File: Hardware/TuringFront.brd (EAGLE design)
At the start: 107 x 49.5 mm, 66 parts, among them T1 2N3904, U1 TL074_

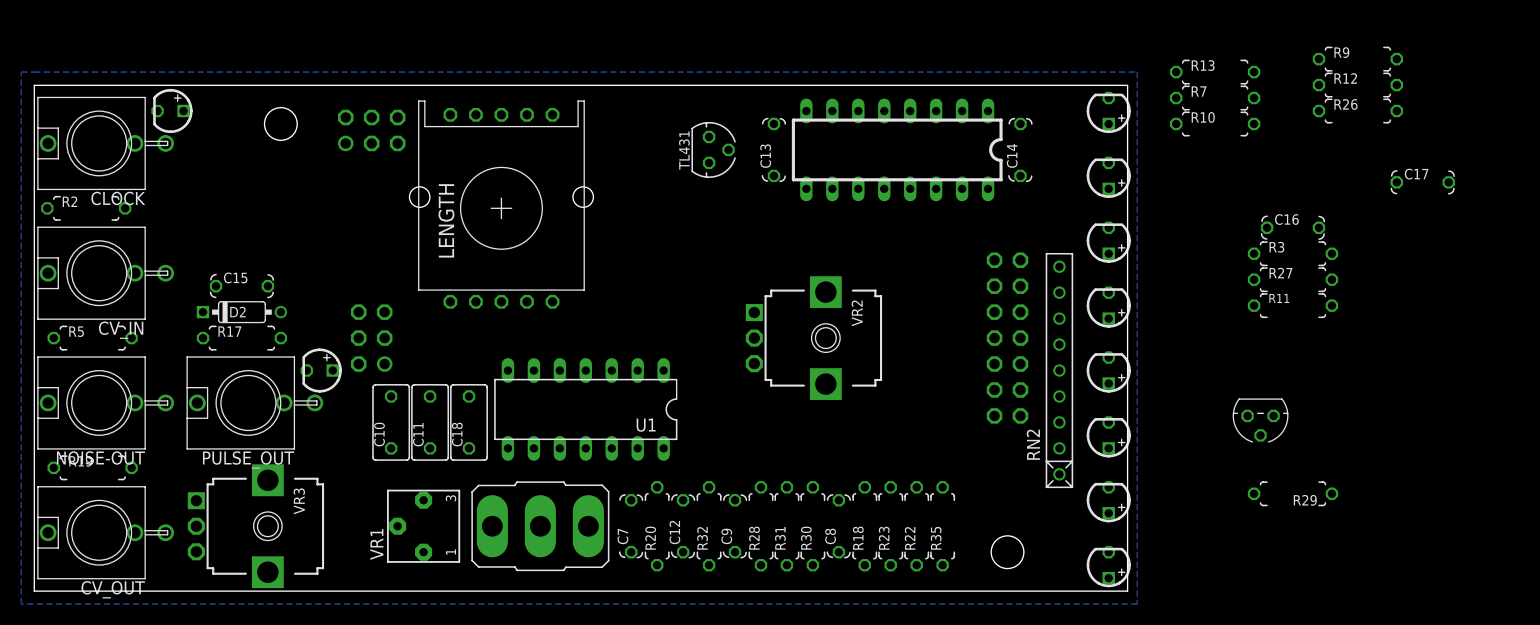
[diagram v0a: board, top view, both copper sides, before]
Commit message: Starting to route front board
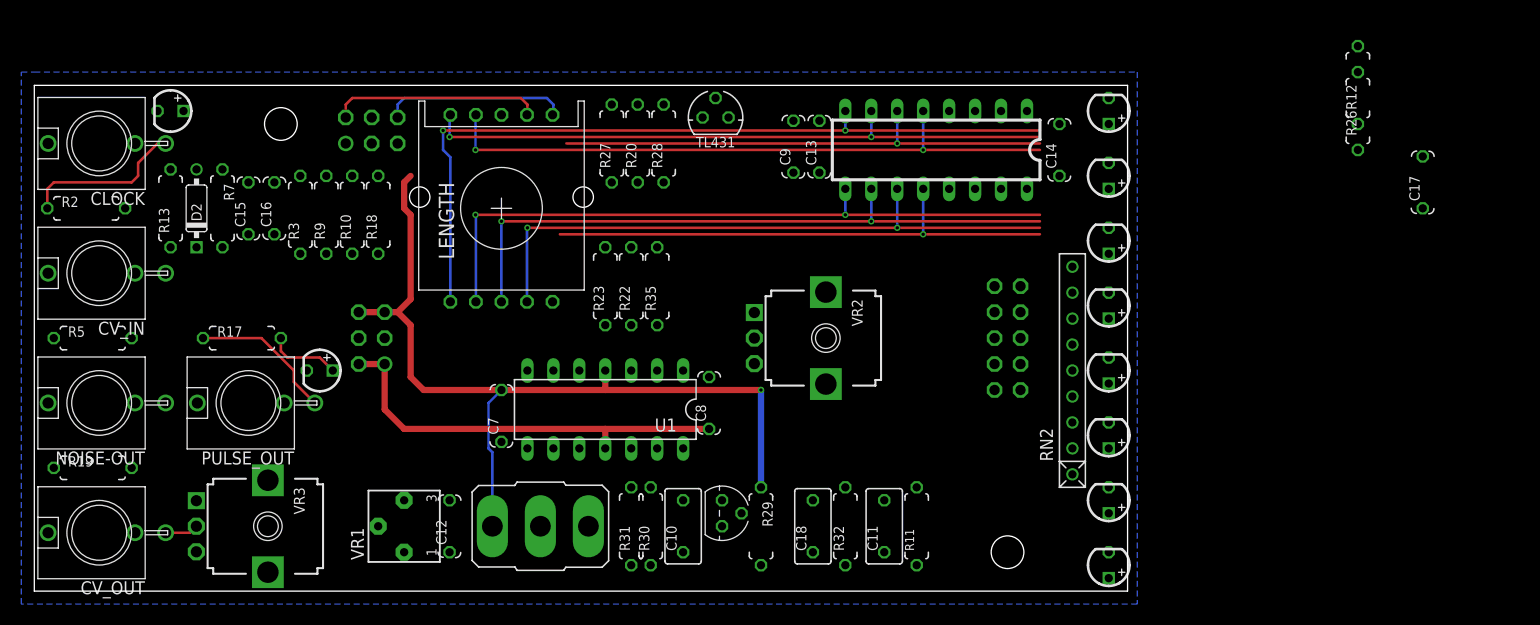
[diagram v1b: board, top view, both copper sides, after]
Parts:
- removed FRONT_BUS: (no value), MusicThingModular:MA07-2_BACKSIDE
- added SV1: (no value), MusicThingModular:10PIN_BACKSIDE
- moved R13 103.1 mm to (13.3, 37.5), turned to 90 degrees
- moved R9 102.1 mm to (28.6, 36.8), turned to 90 degrees
- moved C16 99.7 mm to (23.5, 37.5), turned to 90 degrees
- moved R7 97.8 mm to (18.4, 37.5), turned to 270 degrees
- moved R3 97.2 mm to (26.0, 36.8), turned to 90 degrees
- moved R10 84.9 mm to (31.1, 36.8), turned to 90 degrees
- moved R27 68.0 mm to (56.5, 43.8), turned to 90 degrees
- moved R18 56.5 mm to (33.7, 36.8)
- moved T1 53.6 mm to (67.3, 7.62), turned to 270 degrees
- moved R29 52.2 mm to (71.1, 6.35), turned to 270 degrees
- moved C11 45.6 mm to (83.2, 6.35)
- moved R11 42.7 mm to (86.4, 6.35), turned to 90 degrees
- moved R28 38.7 mm to (61.6, 43.8)
- moved C9 37.6 mm to (74.3, 43.5)
- moved R20 37.5 mm to (59.1, 43.8)
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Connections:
- net +12V_FRONT: now also C7.2, R20.1, R23.2, R29.1, R3.1; no longer C7.1, R20.2, R23.1, R29.2, R3.2
- net -12V_FRONT: now also C14.2, C8.1, C9.2, R35.2; no longer C14.1, C8.2, C9.1, R35.1
- net B1_FRONT: now also SV1.1; no longer FRONT_BUS.1
- net B2_FRONT: now also SV1.2; no longer FRONT_BUS.2
- net B3_FRONT: now also SV1.3; no longer FRONT_BUS.3
- net B4_FRONT: now also SV1.4; no longer FRONT_BUS.4
- net B5_FRONT: now also SV1.5; no longer FRONT_BUS.5
- net B6_FRONT: now also SV1.6; no longer FRONT_BUS.6
- net B7_FRONT: now also SV1.7; no longer FRONT_BUS.7
- net B8_FRONT: now also SV1.8; no longer FRONT_BUS.8
- net CLOCK_FRONT: now also R13.1, SV1.9; no longer FRONT_BUS.9, R13.2
- net GND_FRONT: now also C14.1, C16.1, C7.1, C8.2, R11.1, R9.1, U1.12; no longer C14.2, C16.2, C7.2, C8.1, R11.2, R9.2, U1.5
- net LOOP_CTRL_FRONT: now also R22.2; no longer R22.1
- net MAIN_OUT: now also U1.1; no longer U1.8
- net N$12: now also C16.2, R3.2, R9.2, U1.6; no longer C16.1, R3.1, R9.1, U1.13
- net N$13: now also U1.2; no longer U1.9
- net N$15: now also R13.2; no longer R13.1
- net N$16: now also C10.2, R29.2; no longer C10.1, R29.1
- net N$18: now also R20.2, R28.2; no longer R20.1, R28.1
- net N$20: now also C10.1; no longer C10.2
- net N$21: now also U1.9; no longer U1.2
- net N$22: now also U1.8; no longer U1.1
- net N$25: now also C9.1; no longer C9.2
- net N$26: now also R28.1; no longer R28.2
- net N$27: now also R32.1, U1.13; no longer R32.2, U1.6
- net N$41: now also U1.14; no longer U1.7
- net N$43: now also R22.1; no longer R22.2
- net N$47: now also R23.1; no longer R23.2
- net N$48: now also R35.1; no longer R35.2
- net N$5: now also U1.5; no longer U1.12
- net N$6: now also R17.2; no longer R17.1
- net N$8: now also U1.7; no longer U1.14
- net N$9: now also R32.2; no longer R32.1
- net NOISE_FRONT: now also R11.2; no longer R11.1
- net PULSE_OUT_FRONT: now also R17.1, SV1.10; no longer FRONT_BUS.10, R17.2
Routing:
- net +12V_FRONT: track 0.00 -> 85.3 mm, vias 0 -> 1
- net B4_FRONT: track 0.00 -> 77.4 mm, vias 0 -> 2
- net B5_FRONT: track 0.00 -> 66.3 mm, vias 0 -> 2
- net B6_FRONT: track 0.00 -> 63.8 mm, vias 0 -> 2
- net B3_FRONT: track 0.00 -> 62.5 mm, vias 0 -> 2
- net B1_FRONT: track 0.00 -> 62.5 mm, vias 0 -> 2
- net B7_FRONT: track 0.00 -> 61.2 mm, vias 0 -> 2
- net B8_FRONT: track 0.00 -> 51.4 mm, vias 0 -> 1
- net B2_FRONT: track 0.00 -> 49.5 mm, vias 0 -> 1
- net -12V_FRONT: track 0.00 -> 41.4 mm
- net STEP_16_FRONT: track 0.00 -> 20.6 mm
- net END_OF_LOOP_FRONT: track 0.00 -> 18.1 mm
- net N$2: track 0.00 -> 16.1 mm
- net PULSE_OUT_FRONT: track 0.00 -> 14.2 mm
- net N$6: track 0.00 -> 7.14 mm
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
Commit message: Layouts
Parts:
- removed RN2: 2.2k, resistor-net:RN-9
- added R1, R14, R15, R16, R21, R4, R6, R8: 2.2k, TomW:0207/7
- moved R12 111.8 mm to (18.4, 37.5)
- moved C7 73.4 mm to (116.2, 37.5)
- moved C13 70.5 mm to (144.1, 22.5)
- moved TL431 70.5 mm to (134.0, 25.4)
- moved R20 70.5 mm to (126.4, 22.9)
- moved R27 70.5 mm to (123.8, 22.9)
- moved R28 70.5 mm to (128.9, 22.9)
- moved C9 70.5 mm to (141.6, 22.5)
- moved R29 59.7 mm to (130.8, 7.62)
- moved C10 59.1 mm to (122.6, 7.62)
- moved T1 59.1 mm to (126.4, 8.89)
- moved R30 58.4 mm to (118.7, 7.62)
- moved C8 58.0 mm to (120.7, 38.1)
- moved C18 57.8 mm to (134.0, 7.62)
- moved R11 57.8 mm to (144.1, 7.62)
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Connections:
- net CLOCK_FRONT: now also R12.1, R7.1; no longer R12.2, R7.2
- net GND_FRONT: now also R1.2, R12.2, R14.1, R15.1, R16.1, R21.1, R4.2, R6.2, R8.2; no longer R12.1, RN2.1
- net N$30: now also R1.1; no longer RN2.9
- net N$31: now also R4.1; no longer RN2.8
- net N$32: now also R6.1; no longer RN2.7
- net N$33: now also R8.1; no longer RN2.6
- net N$34: now also R14.2; no longer RN2.5
- net N$35: now also R15.2; no longer RN2.4
- net N$36: now also R16.2; no longer RN2.3
- net N$37: now also R21.2; no longer RN2.2
- net N$5: now also R7.2; no longer R7.1
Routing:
- net +12V_FRONT: track 85.3 -> 0.00 mm, vias 1 -> 0
- net B4_FRONT: track 77.4 -> 0.00 mm, vias 2 -> 0
- net B5_FRONT: track 66.3 -> 0.00 mm, vias 2 -> 0
- net B6_FRONT: track 63.8 -> 0.00 mm, vias 2 -> 0
- net B3_FRONT: track 62.5 -> 0.00 mm, vias 2 -> 0
- net B1_FRONT: track 62.5 -> 0.00 mm, vias 2 -> 0
- net B7_FRONT: track 61.2 -> 0.00 mm, vias 2 -> 0
- net MAIN_OUT: track 0.00 -> 60.0 mm
- net B8_FRONT: track 51.4 -> 0.00 mm, vias 1 -> 0
- net PULSE_OUT_FRONT: track 14.2 -> 65.5 mm
- net B2_FRONT: track 49.5 -> 0.00 mm, vias 1 -> 0
- net -12V_FRONT: track 41.4 -> 0.00 mm
- net LOOP_CTRL_FRONT: track 0.00 -> 30.5 mm
- net NOISE_FRONT: track 0.00 -> 23.8 mm
- net STEP_16_FRONT: track 20.6 -> 0.00 mm
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
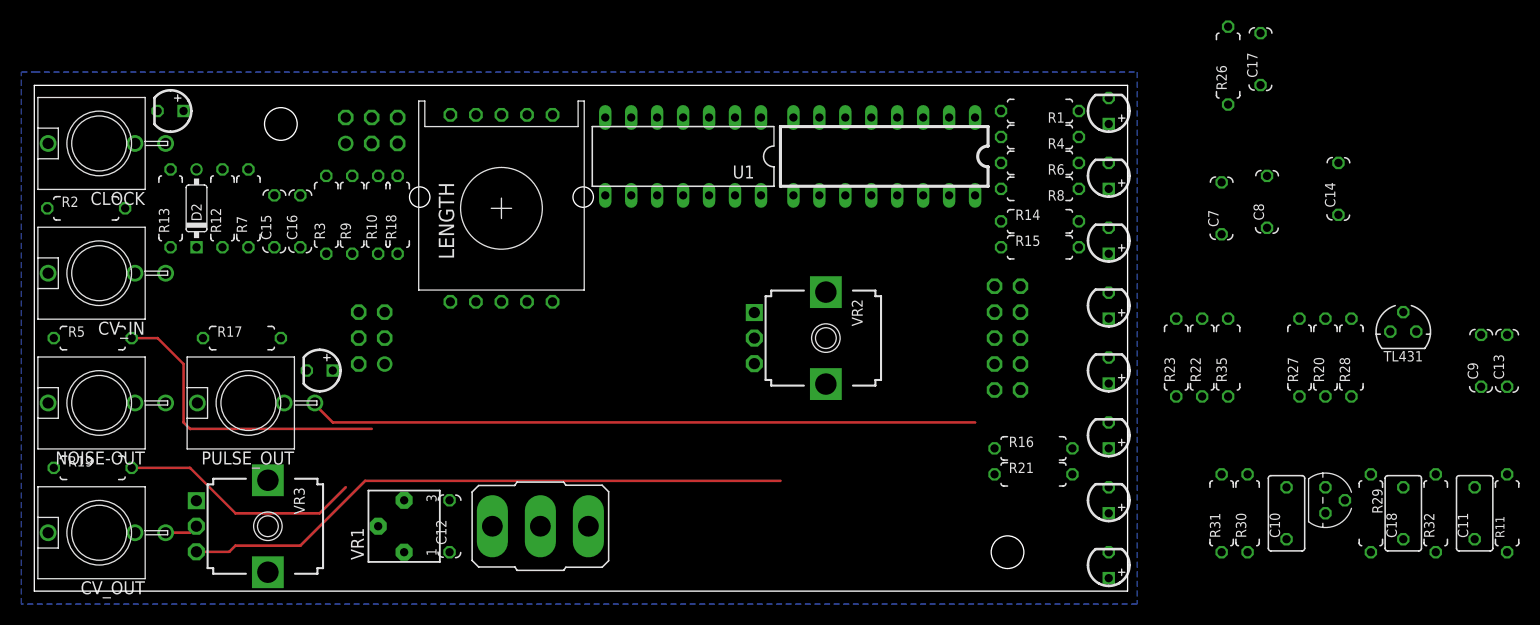
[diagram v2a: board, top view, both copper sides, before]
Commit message: routing tweaks on back panel
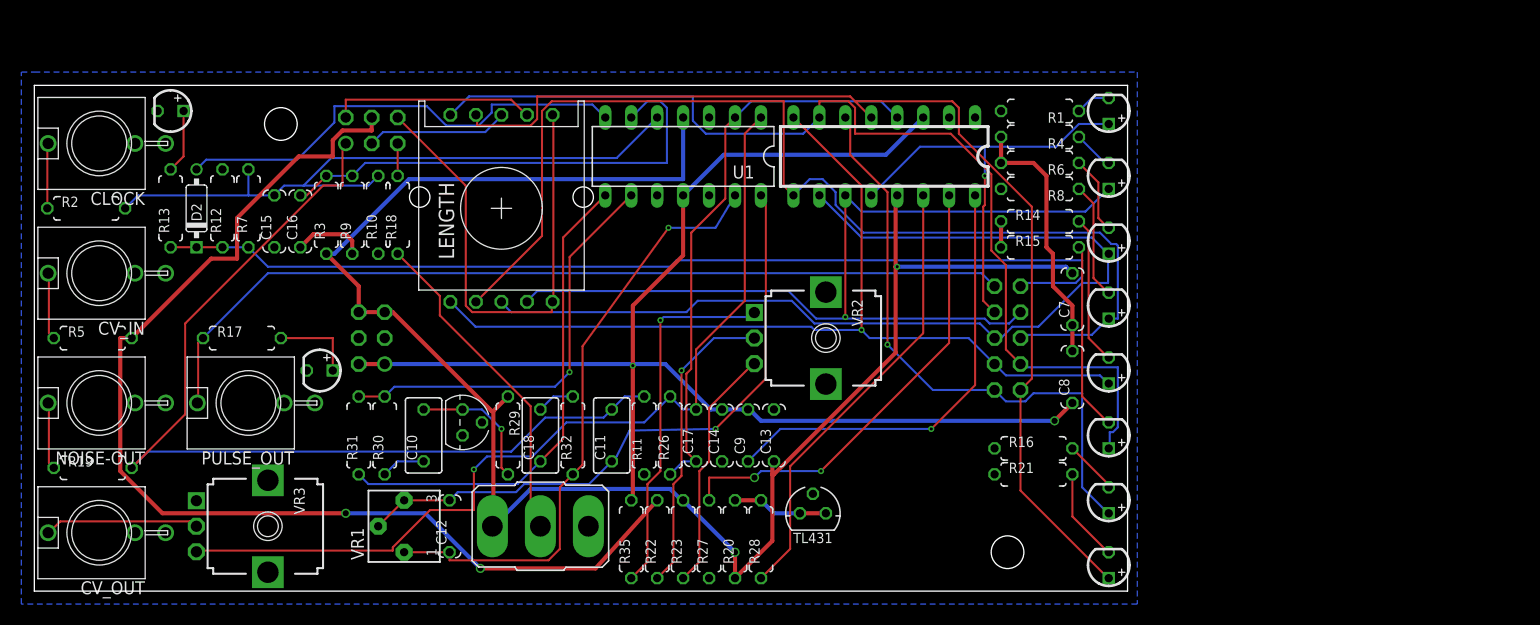
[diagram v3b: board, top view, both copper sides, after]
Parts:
- moved C10 84.8 mm to (38.1, 15.2)
- moved C18 84.8 mm to (49.5, 15.2)
- moved R11 84.8 mm to (59.7, 15.2)
- moved R29 84.8 mm to (46.4, 15.2)
- moved R30 84.8 mm to (34.3, 15.2)
- moved C11 84.8 mm to (56.5, 15.2)
- moved R31 84.8 mm to (31.8, 15.2)
- moved R32 84.8 mm to (52.7, 15.2)
- moved T1 84.8 mm to (41.9, 16.5)
- moved C13 72.1 mm to (72.4, 15.2)
- moved C9 72.1 mm to (69.8, 15.2)
- moved C17 66.4 mm to (64.8, 15.2)
- moved R26 65.5 mm to (62.2, 15.2)
- moved C14 65.0 mm to (67.3, 15.2)
- moved R35 61.1 mm to (58.4, 5.08)
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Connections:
- net GND_FRONT: now also CLOCK.P$3_SLEEVE, CV_IN.P$3_SLEEVE, CV_OUT.P$3_SLEEVE, NOISE-OUT.P$3_SLEEVE, PULSE_OUT.P$3_SLEEVE, VR2.CHASSIS2, VR3.CHASSIS2; no longer CLOCK.P$1, CV_IN.P$1, CV_OUT.P$1, NOISE-OUT.P$1, PULSE_OUT.P$1, VR2.M1, VR2.M2, VR3.M1, VR3.M2
- net N$2: now also CLOCK.P$1_TIP; no longer CLOCK.P$3
- net N$3: now also CV_IN.P$1_TIP; no longer CV_IN.P$3
- net N$39: now also CV_OUT.P$1_TIP; no longer CV_OUT.P$3
- net N$40: now also NOISE-OUT.P$1_TIP; no longer NOISE-OUT.P$3
- net PULSE_OUT_FRONT: now also PULSE_OUT.P$1_TIP; no longer PULSE_OUT.P$3
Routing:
- net +12V_FRONT: track 0.00 -> 175.0 mm, vias 0 -> 2
- net -12V_FRONT: track 0.00 -> 131.6 mm, vias 0 -> 2
- net B5_FRONT: track 0.00 -> 108.3 mm
- net B1_FRONT: track 0.00 -> 106.5 mm
- net B3_FRONT: track 0.00 -> 101.2 mm
- net CLOCK_FRONT: track 0.00 -> 98.3 mm
- net B6_FRONT: track 0.00 -> 97.6 mm
- net B4_FRONT: track 0.00 -> 91.3 mm, vias 0 -> 1
- net B7_FRONT: track 0.00 -> 90.0 mm, vias 0 -> 1
- net LOOP_CTRL_FRONT: track 30.5 -> 110.0 mm, vias 0 -> 2
- net NOISE_FRONT: track 23.8 -> 94.6 mm
- net N$5: track 0.00 -> 66.0 mm
- net N$41: track 0.00 -> 62.5 mm, vias 0 -> 1
- net N$27: track 0.00 -> 59.9 mm, vias 0 -> 1
- net B2_FRONT: track 0.00 -> 58.5 mm, vias 0 -> 1
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
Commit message: Front board routed awaiting checking and optimisation
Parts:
- moved C8 26.2 mm to (98.4, 47.0), turned to 0 degrees
- moved R15 19.7 mm to (97.8, 14.0)
- moved R14 19.7 mm to (97.8, 16.5)
- moved C7 16.2 mm to (98.4, 44.5), turned to 180 degrees
- moved R1 5.08 mm to (98.4, 41.9)
- moved R4 5.08 mm to (98.4, 39.4)
- moved R6 5.08 mm to (98.4, 36.8)
- moved R8 5.08 mm to (98.4, 34.3)
- moved R16 2.54 mm to (97.8, 11.4)
- moved R21 2.54 mm to (97.8, 8.89)
- moved T1 1.90 mm to (41.9, 18.4), turned to 0 degrees
- moved C10 1.27 mm to (36.8, 15.2)
- moved R20 1.27 mm to (69.8, 5.08)
- moved R22 1.27 mm to (62.2, 5.08)
- moved R23 1.27 mm to (64.8, 5.08)
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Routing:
- net B5_FRONT: track 108.3 -> 81.2 mm, vias 0 -> 3
- net GND_FRONT: track 35.4 -> 9.72 mm
- net N$11: track 32.5 -> 48.0 mm
- net N$35: track 18.4 -> 4.61 mm
- net MAIN_OUT: track 89.5 -> 101.5 mm, vias 1 -> 3
- net END_OF_LOOP_FRONT: track 49.3 -> 37.4 mm
- net N$21: track 41.4 -> 53.0 mm
- net B7_FRONT: track 90.0 -> 78.7 mm, vias 1 -> 3
- net CLOCK_FRONT: track 98.3 -> 87.2 mm
- net B6_FRONT: track 97.6 -> 87.8 mm, vias 0 -> 3
- net LOOP_CTRL_FRONT: track 110.0 -> 100.3 mm
- net N$12: track 47.0 -> 38.0 mm
- net N$26: track 44.0 -> 51.0 mm, vias 0 -> 1
- net N$25: track 43.9 -> 50.7 mm
- net B8_FRONT: track 42.9 -> 49.3 mm, vias 1 -> 2
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
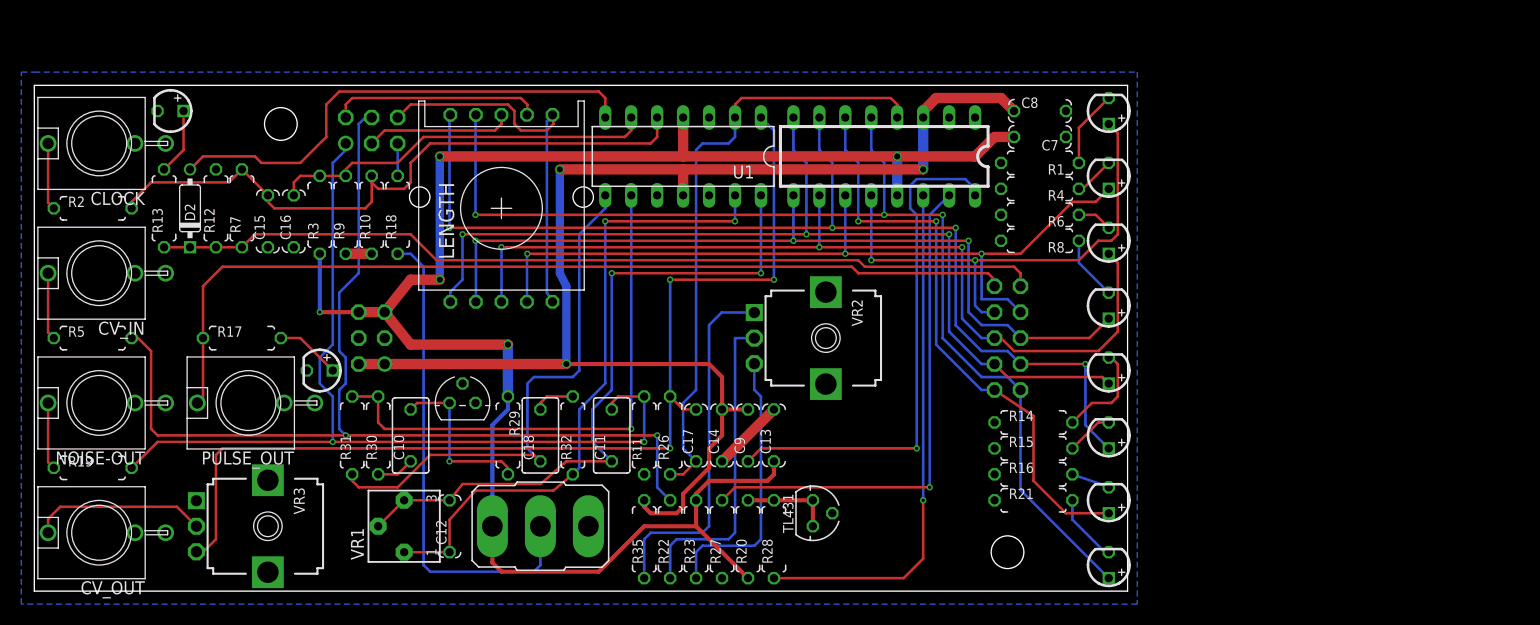
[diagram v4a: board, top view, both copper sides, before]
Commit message: clean up front layout
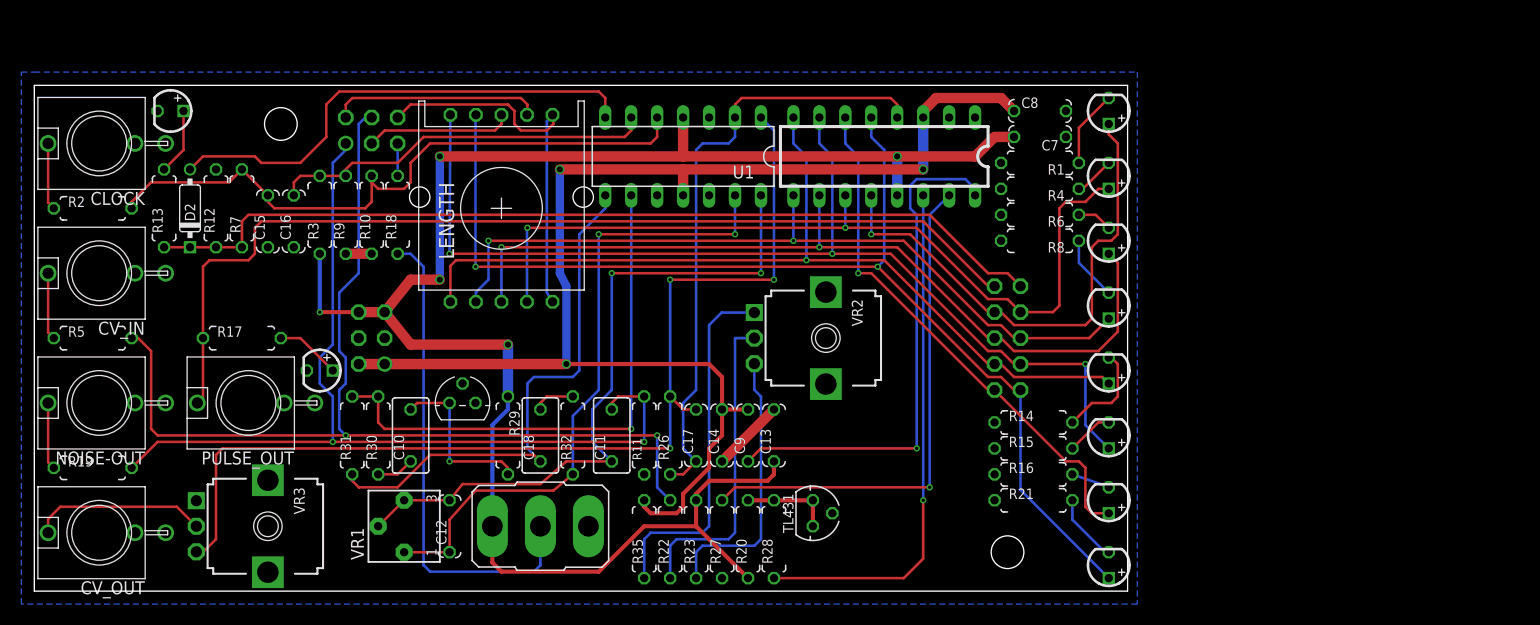
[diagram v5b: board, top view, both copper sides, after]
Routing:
- net B4_FRONT: track 93.9 -> 87.7 mm, vias 3 -> 1
- net PULSE_OUT_FRONT: track 91.1 -> 97.0 mm
- net B2_FRONT: track 57.5 -> 52.2 mm, vias 2 -> 1
- net B5_FRONT: track 81.2 -> 76.4 mm, vias 3 -> 2
- net B6_FRONT: track 87.8 -> 83.7 mm, vias 3 -> 2
- net B7_FRONT: track 78.7 -> 81.3 mm, vias 3 -> 2
- net CLOCK_FRONT: track 87.2 -> 89.5 mm
- net B3_FRONT: track 104.9 -> 103.4 mm, vias 4 -> 3
- net B1_FRONT: track 109.4 -> 110.6 mm, vias 3 -> 2
- net B8_FRONT: track 49.3 -> 50.6 mm, vias 2 -> 1
